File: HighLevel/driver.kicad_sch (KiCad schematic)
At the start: 41 parts, among them J1 UCC27210DDA, J2 UCC27210DDA, J3 UCC27210DDA, U1 MCP16311MS, U2 MCP16311MS, U3 MC74VHC1GT66, U4 MC74VHC1GT66, U5 MC74VHC1GT66

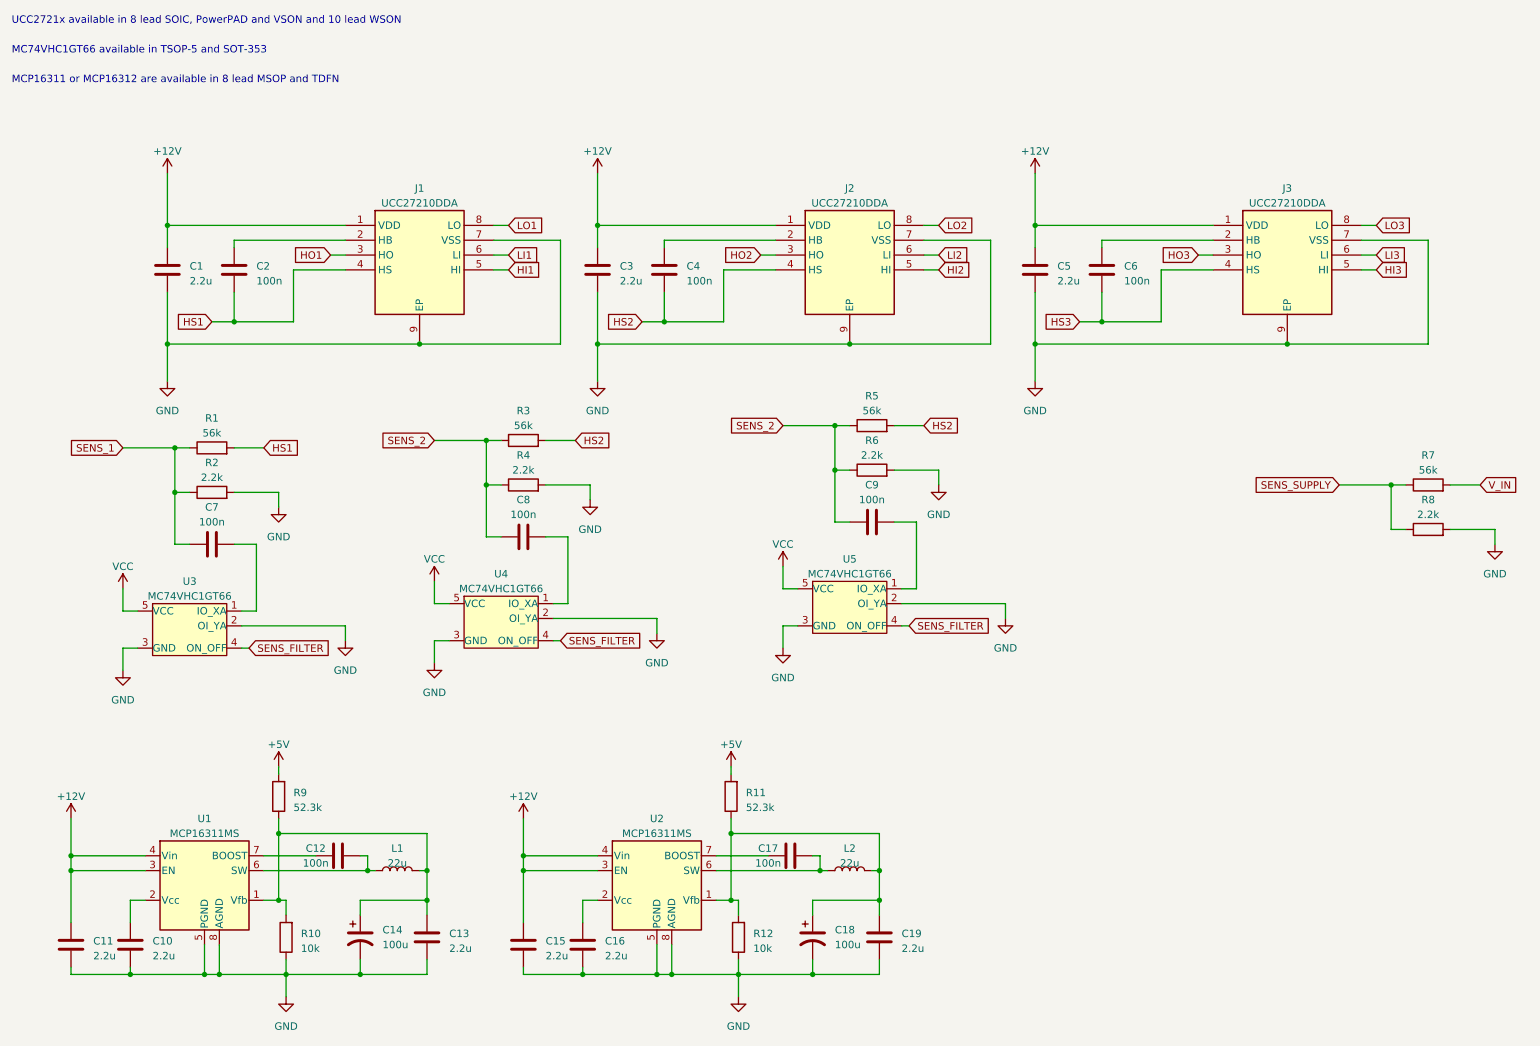
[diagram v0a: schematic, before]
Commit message: added footprints and changed to hierarchical labels
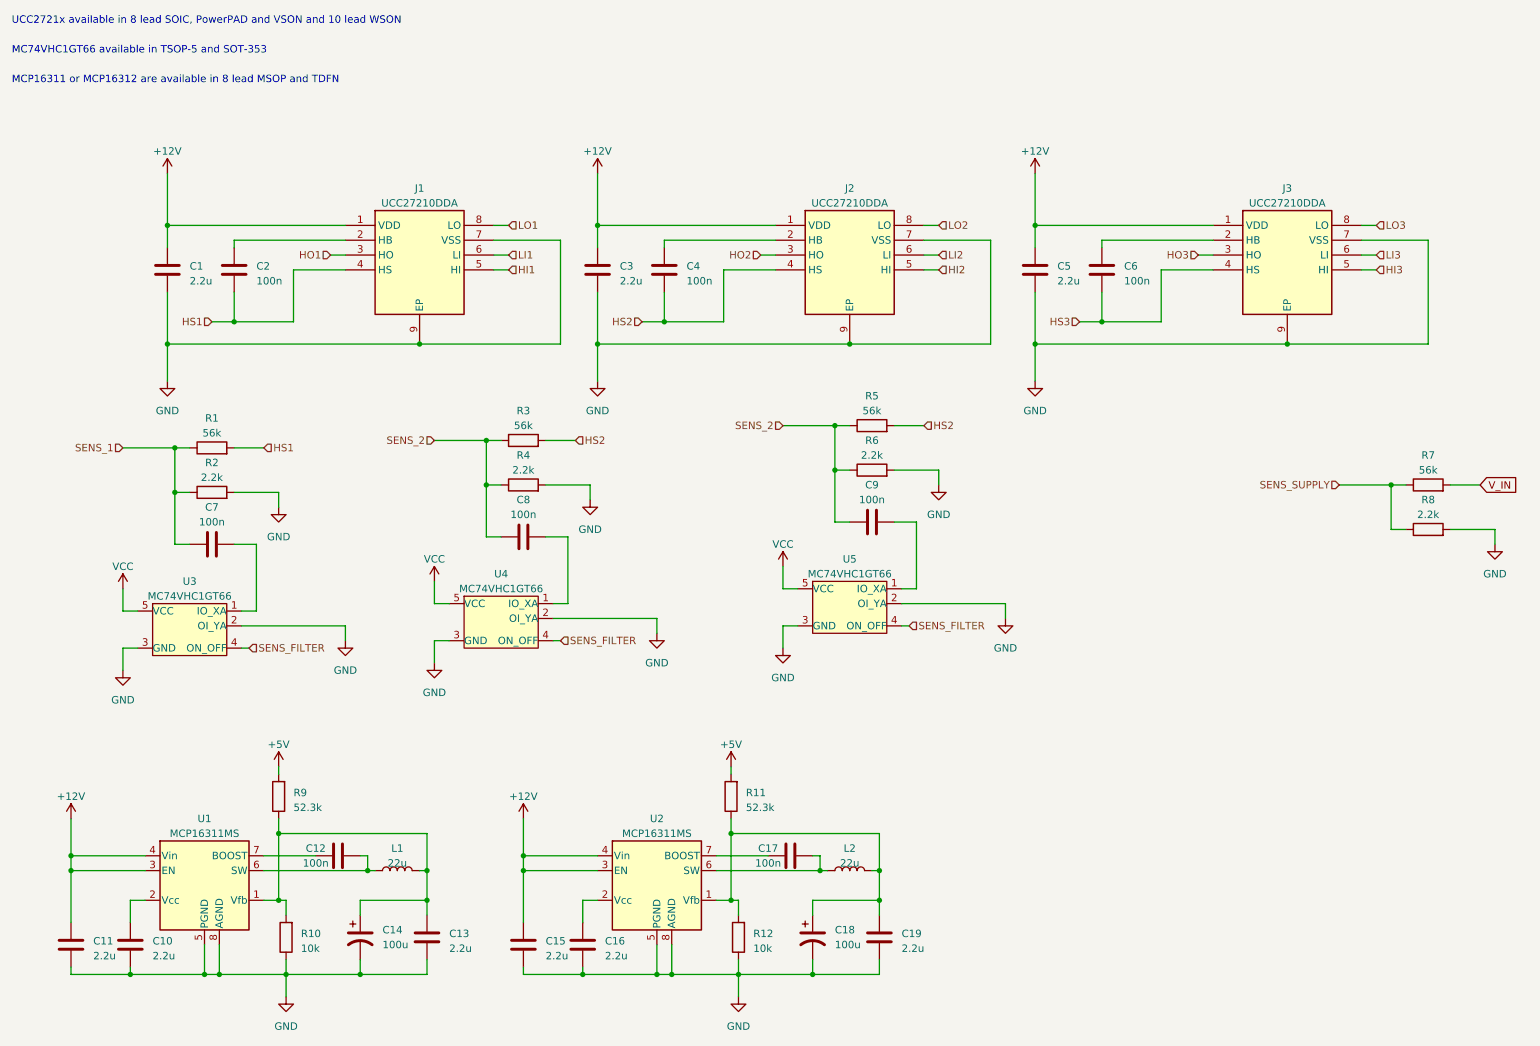
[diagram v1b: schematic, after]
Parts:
- C1, C10, C11, C12, C13, C15, C16, C17, C19, C2, C3, C4, C5, C6, C7, C8, C9: footprint (none) -> Capacitor_SMD:C_0805_2012Metric
- C14, C18: footprint (none) -> Capacitor_SMD:CP_Elec_6.3x7.7
- J1, J2, J3: footprint SOIC127P600X170-9N -> Package_SO:SOIC-8-1EP_3.9x4.9mm_P1.27mm_EP2.41x3.3mm
- L1, L2: footprint (none) -> Inductor_SMD:L_0805_2012Metric
- R1, R10, R11, R12, R2, R3, R4, R5, R6, R7, R8, R9: footprint (none) -> Resistor_SMD:R_0805_2012Metric
- U3, U4, U5: footprint (none) -> Package_TO_SOT_SMD:SOT-353_SC-70-5
